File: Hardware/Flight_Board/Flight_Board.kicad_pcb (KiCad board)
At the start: 2 copper layers, 50.8 x 101.6 mm, 128 parts, among them J1 Conn_01x04, J2 Conn_01x08, J3 Conn_01x04, J4 Conn_01x06, J5 MEM2067-02-180-00-A_REVB, SW1 SW_Push, U1 FT5HN, U2 STM32F411RCTx, U3 ADXL375, U4 BMP390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

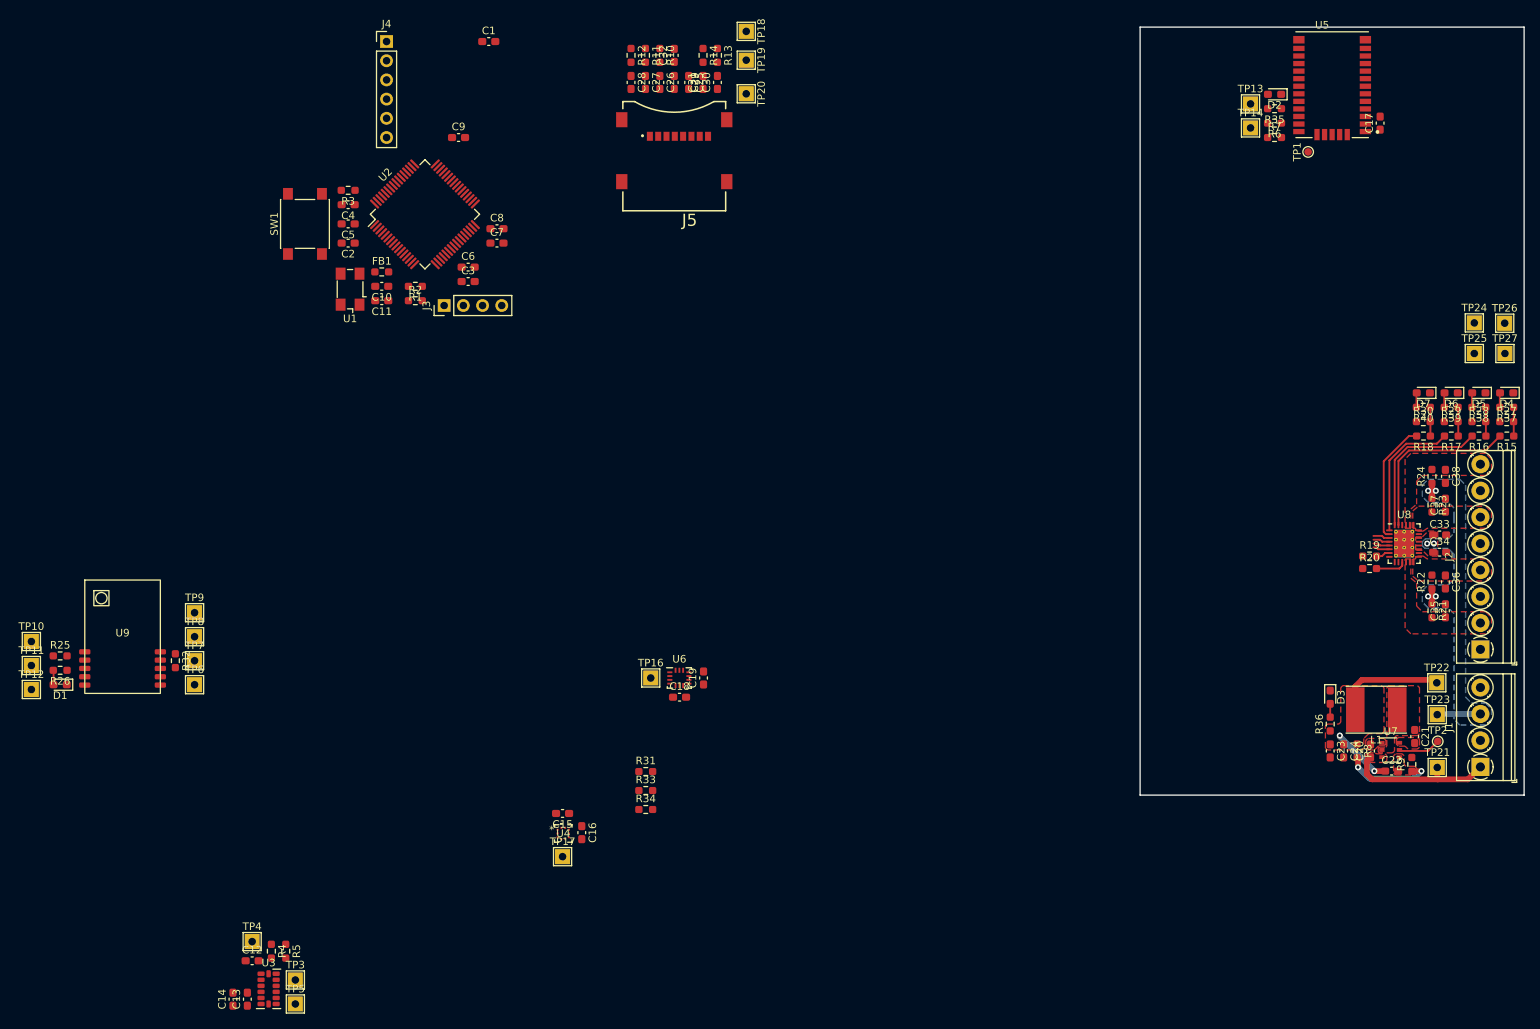
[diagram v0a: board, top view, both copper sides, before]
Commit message: initial placement on board, continue routing
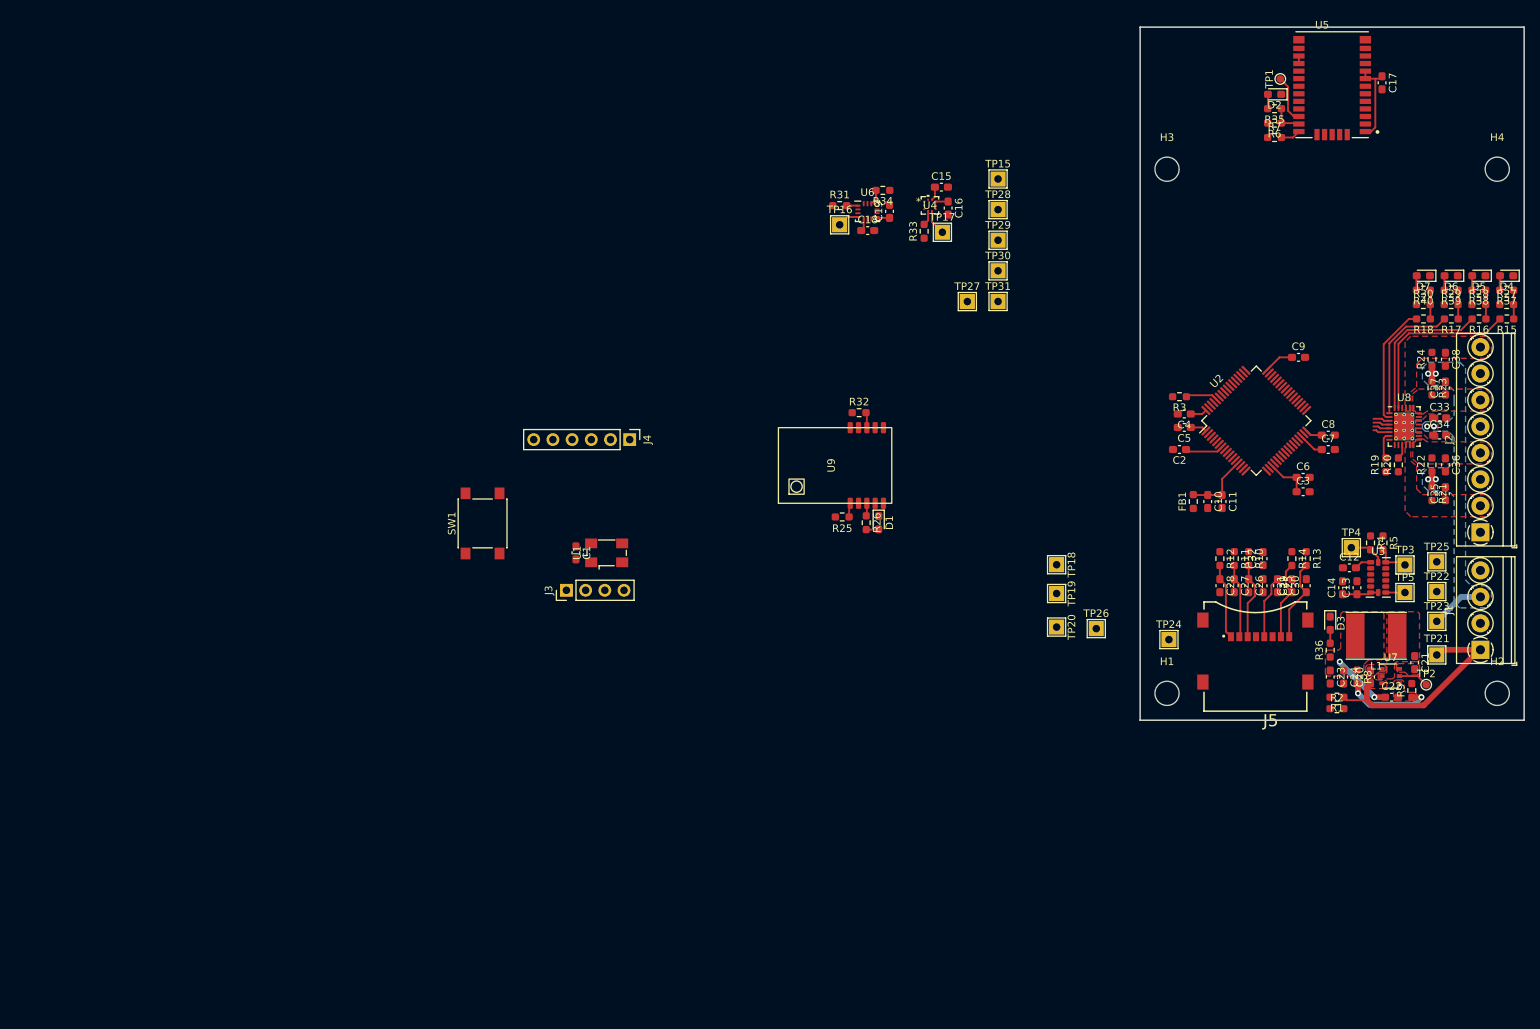
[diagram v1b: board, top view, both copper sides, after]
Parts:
- removed TP10: RST, TestPoint:TestPoint_THTPad_2.0x2.0mm_Drill1.0mm
- removed TP11: BUSY, TestPoint:TestPoint_THTPad_2.0x2.0mm_Drill1.0mm
- removed TP12: DIO1, TestPoint:TestPoint_THTPad_2.0x2.0mm_Drill1.0mm
- removed TP13: TX, TestPoint:TestPoint_THTPad_2.0x2.0mm_Drill1.0mm
- removed TP14: RX, TestPoint:TestPoint_THTPad_2.0x2.0mm_Drill1.0mm
- removed TP6: SCK, TestPoint:TestPoint_THTPad_2.0x2.0mm_Drill1.0mm
- removed TP7: MOSI, TestPoint:TestPoint_THTPad_2.0x2.0mm_Drill1.0mm
- removed TP8: MISO, TestPoint:TestPoint_THTPad_2.0x2.0mm_Drill1.0mm
- removed TP9: NSS, TestPoint:TestPoint_THTPad_2.0x2.0mm_Drill1.0mm
- added H1: MountingHole, MountingHole:MountingHole_3.2mm_M3, F.Cu at (232.2, 113.5)
- added H2: MountingHole, MountingHole:MountingHole_3.2mm_M3, F.Cu at (275.8, 113.5)
- added H3: MountingHole, MountingHole:MountingHole_3.2mm_M3, F.Cu at (232.2, 44.2)
- added H4: MountingHole, MountingHole:MountingHole_3.2mm_M3, F.Cu at (275.8, 44.2)
- added TP15: MISO, TestPoint:TestPoint_THTPad_2.0x2.0mm_Drill1.0mm, F.Cu at (209.8, 45.5)
- added TP28: MOSI, TestPoint:TestPoint_THTPad_2.0x2.0mm_Drill1.0mm, F.Cu at (209.8, 49.5)
- added TP29: SCK, TestPoint:TestPoint_THTPad_2.0x2.0mm_Drill1.0mm, F.Cu at (209.8, 53.6)
- added TP30: CS1, TestPoint:TestPoint_THTPad_2.0x2.0mm_Drill1.0mm, F.Cu at (209.8, 57.6)
- added TP31: CS2, TestPoint:TestPoint_THTPad_2.0x2.0mm_Drill1.0mm, F.Cu at (209.8, 61.7)
- moved TP3 156.7 mm to (263.6, 96.6)
- moved C13 156.6 mm to (257.3, 99.6)
- moved C14 156.6 mm to (255.4, 99.6)
- moved TP5 156.6 mm to (263.6, 100.2)
- moved U3 156.6 mm to (260.1, 98.2)
- moved R4 155.1 mm to (259.1, 93.6)
- moved R5 154.9 mm to (260.7, 93.6)
- moved TP4 154.5 mm to (256.5, 94.3)
- moved C12 154.2 mm to (256.3, 96.9)
- moved R1 133.5 mm to (254.6, 114.0)
- moved R2 133.3 mm to (254.6, 115.6)
- moved C9 114.9 mm to (249.6, 69.1)
- moved C11 114.3 mm to (239.4, 88.2), turned to -90 degrees
- moved C4 114.0 mm to (234.4, 76.6)
- moved C3 113.9 mm to (250.2, 86.9)
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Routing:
- net +3.3V: track 22.4 -> 50.0 mm
- net /MicroSD/SDIO_D1: track 0.00 -> 11.0 mm
- net /MicroSD/SDIO_D0: track 0.00 -> 10.7 mm
- net /MicroSD/SDIO_CMD: track 0.00 -> 10.1 mm
- net /VBAT: track 20.0 -> 30.0 mm
- net /MicroSD/SDIO_D2: track 0.00 -> 10.0 mm
- net /MicroSD/SDIO_D3: track 0.00 -> 9.80 mm
- net Net-(U2-VDDA): track 0.00 -> 9.00 mm
- net /MicroSD/SDIO_CLK: track 0.00 -> 8.33 mm
- net Net-(U5-SAFEBOOT_N): track 0.00 -> 6.37 mm
- net /Microcontroller/NRST: track 0.00 -> 5.11 mm
- net /Accelerometer/SCL: track 0.00 -> 4.74 mm
- net /Accelerometer/SDA: track 0.00 -> 4.69 mm
- net Net-(U2-BOOT0): track 0.00 -> 4.32 mm
- net Net-(U5-TXD/SPI_MISO): track 0.00 -> 4.26 mm
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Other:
- board size 50.8 x 101.6 mm -> 50.8 x 91.7 mm

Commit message: flip mcu pins around, improve routability
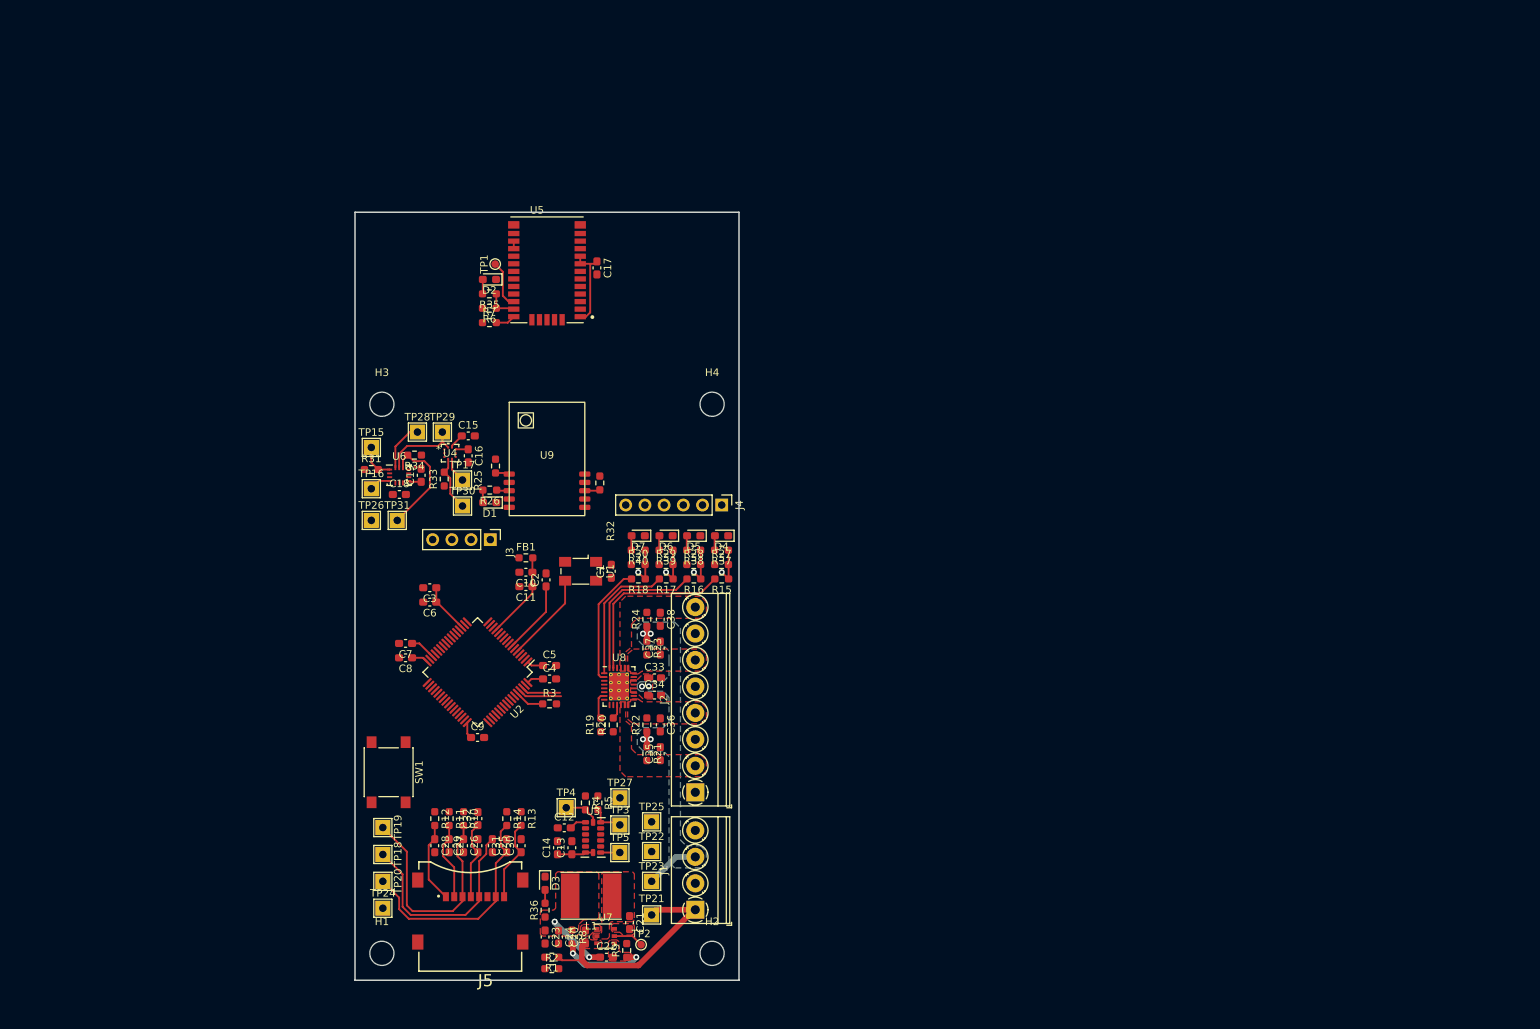
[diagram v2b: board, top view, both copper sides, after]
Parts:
- moved C8 125.6 mm to (131.4, 108.8), turned to 180 degrees
- moved C7 124.7 mm to (131.4, 106.9), turned to 180 degrees
- moved C9 119.7 mm to (140.9, 119.4)
- moved C6 116.7 mm to (134.6, 101.5), turned to 180 degrees
- moved C3 116.2 mm to (134.6, 99.6), turned to 180 degrees
- moved TP24 109.9 mm to (128.4, 142.0)
- moved C21 109.4 mm to (161.1, 143.9)
- moved C22 109.4 mm to (158.0, 148.4)
- moved D4 109.4 mm to (173.2, 92.7)
- moved D5 109.4 mm to (169.5, 92.7)
- moved R19 109.4 mm to (157.2, 117.7)
- moved R21 109.4 mm to (163.3, 121.5)
- moved R22 109.4 mm to (163.3, 117.7)
- moved R23 109.4 mm to (163.3, 107.5)
- moved R24 109.4 mm to (163.3, 103.7)
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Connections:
- U2 pad 10: /Barometer/MISO -> /Current Switch/EN3
- U2 pad 11: /Barometer/MOSI -> /Current Switch/EN4
- U2 pad 2: /Current Switch/~{ST2} -> unconnected-(U2-PC13-Pad2)
- U2 pad 24: /Barometer/~{CS} -> /LoRa/LORA_RST
- U2 pad 25: /IMU/~{CS} -> /LoRa/LORA_BUSY
- U2 pad 26: /LoRa/LORA_BUSY -> /LoRa/LORA_DIO1
- U2 pad 27: /LoRa/LORA_DIO1 -> /Barometer/INT
- U2 pad 28: /LoRa/LORA_RST -> /IMU/INT1
- U2 pad 29: /Barometer/SCK -> unconnected-(U2-PB10-Pad29)
- U2 pad 3: /Current Switch/~{ST3} -> unconnected-(U2-PC14-Pad3)
- U2 pad 34: unconnected-(U2-PB13-Pad34) -> /Barometer/~{CS}
- U2 pad 35: unconnected-(U2-PB14-Pad35) -> /Barometer/MISO
- U2 pad 36: /MicroSD/SDIO_CLK -> /Barometer/MOSI
- U2 pad 37: /Current Switch/EN3 -> /IMU/~{CS}
- U2 pad 38: /Current Switch/EN4 -> /Barometer/SCK
- U2 pad 4: /Current Switch/~{ST4} -> unconnected-(U2-PC15-Pad4)
- U2 pad 41: /Accelerometer/INT1 -> unconnected-(U2-PA8-Pad41)
- U2 pad 44: /IMU/INT1 -> unconnected-(U2-PA11-Pad44)
- U2 pad 45: /Barometer/INT -> unconnected-(U2-PA12-Pad45)
- U2 pad 50: unconnected-(U2-PA15-Pad50) -> /Accelerometer/INT1
- U2 pad 53: /Current Switch/~{ST1} -> /MicroSD/SDIO_CLK
- U2 pad 56: unconnected-(U2-PB4-Pad56) -> /Current Switch/~{ST4}
- U2 pad 57: unconnected-(U2-PB5-Pad57) -> /Current Switch/~{ST3}
- U2 pad 58: /Accelerometer/SCL -> /Current Switch/~{ST2}
- U2 pad 59: /Accelerometer/SDA -> /Current Switch/~{ST1}
- U2 pad 61: unconnected-(U2-PB8-Pad61) -> /Accelerometer/SCL
- U2 pad 62: unconnected-(U2-PB9-Pad62) -> /Accelerometer/SDA
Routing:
- net /MicroSD/SDIO_CMD: track 10.1 -> 30.5 mm
- net /MicroSD/SDIO_CLK: track 8.33 -> 28.4 mm
- net /MicroSD/SDIO_D0: track 10.7 -> 30.1 mm
- net /IMU/~{CS}: track 2.01 -> 14.4 mm
- net /Microcontroller/TCXO_OUT: track 0.00 -> 12.0 mm
- net /Barometer/SCK: track 0.00 -> 10.6 mm
- net +3.3V: track 50.0 -> 58.1 mm
- net /Barometer/MOSI: track 0.00 -> 6.49 mm
- net /Accelerometer/SCL: track 4.74 -> 10.5 mm
- net /Barometer/~{CS}: track 1.98 -> 7.46 mm
- net /Accelerometer/SDA: track 4.69 -> 9.93 mm
- net /Microcontroller/NRST: track 5.11 -> 9.74 mm
- net /Barometer/MISO: track 1.52 -> 4.82 mm
- net Net-(U2-VDDA): track 9.00 -> 11.5 mm
- net /Current Switch/~{ST1}: track 2.22 -> 0.00 mm
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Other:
- board size 50.8 x 91.7 mm -> 50.8 x 101.6 mm

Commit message: Second attempt
Routing complete, check it out
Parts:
- moved C10 1.54 mm to (147.3, 99.1)
- moved C11 1.54 mm to (147.3, 101.0)
- moved FB1 1.54 mm to (147.3, 97.2)
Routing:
- net +3.3V: track 58.1 -> 309.2 mm, vias 2 -> 28
- net /GPS/TXD: track 0.00 -> 60.3 mm, vias 0 -> 2
- net /Microcontroller/VBAT_ADC: track 0.03 -> 59.0 mm, vias 0 -> 2
- net /Microcontroller/SWO: track 0.00 -> 56.3 mm, vias 0 -> 1
- net /Microcontroller/NRST: track 9.74 -> 64.8 mm, vias 0 -> 2
- net /GPS/RXD: track 0.00 -> 54.2 mm, vias 0 -> 2
- net /Barometer/SCK: track 10.6 -> 63.7 mm, vias 0 -> 1
- net /Microcontroller/SWCLK: track 0.00 -> 51.7 mm
- net /Barometer/MOSI: track 6.49 -> 55.7 mm, vias 0 -> 2
- net /Barometer/MISO: track 4.82 -> 52.8 mm, vias 0 -> 2
- net /Microcontroller/SWDIO: track 0.00 -> 47.0 mm, vias 0 -> 1
- net /Current Switch/EN1: track 5.10 -> 44.8 mm, vias 1 -> 2
- net /LoRa/LORA_RST: track 0.00 -> 37.5 mm
- net /LoRa/LORA_BUSY: track 1.70 -> 38.3 mm
- net /Barometer/~{CS}: track 7.46 -> 44.0 mm, vias 0 -> 2
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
